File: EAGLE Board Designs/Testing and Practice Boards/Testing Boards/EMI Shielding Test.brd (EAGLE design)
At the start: 64.8 x 35.6 mm, 25 parts, among them J1 CONNECTOR-5_MICRO_VS_, J2 CONNECTOR-4_μF_S_RA_, U1 VOLTAGE_REGULATOR_ISO_MEE3_05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, U2 ISO224A, U3 VOLTAGE_REGULATOR_SOT-23-5_5V, U4 OPAMP_1_CHANNEL_OPA991

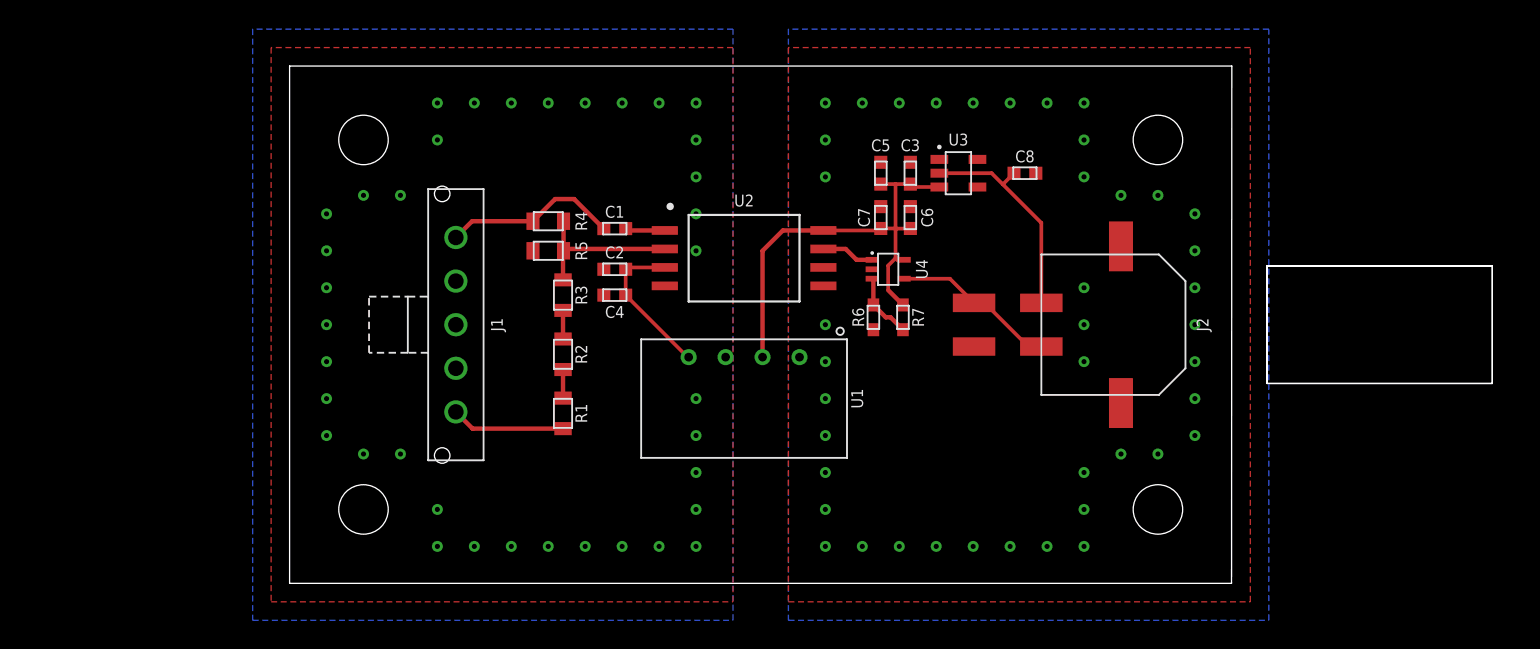
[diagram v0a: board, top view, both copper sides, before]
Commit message: fixed trace width
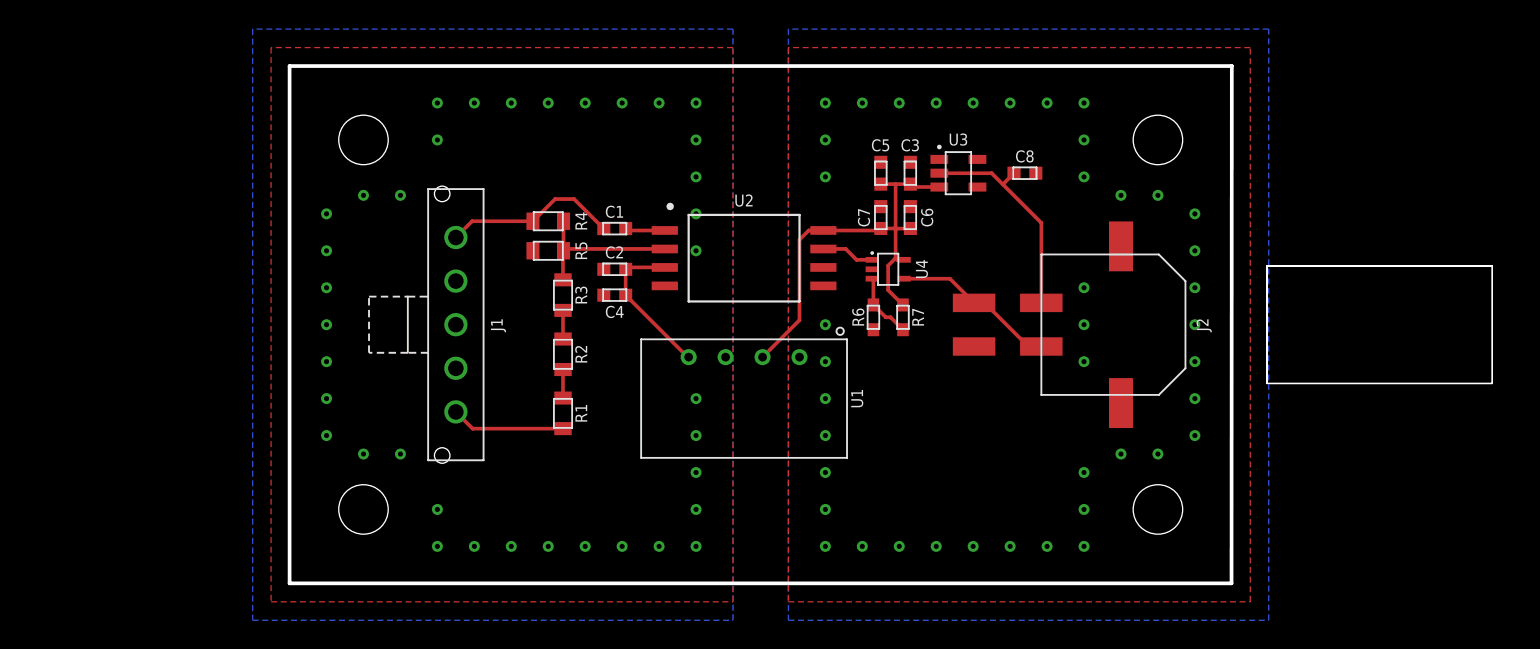
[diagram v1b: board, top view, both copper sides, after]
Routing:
- net +5V: track 31.8 -> 30.8 mm

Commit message: fixed spacing, changed connectors
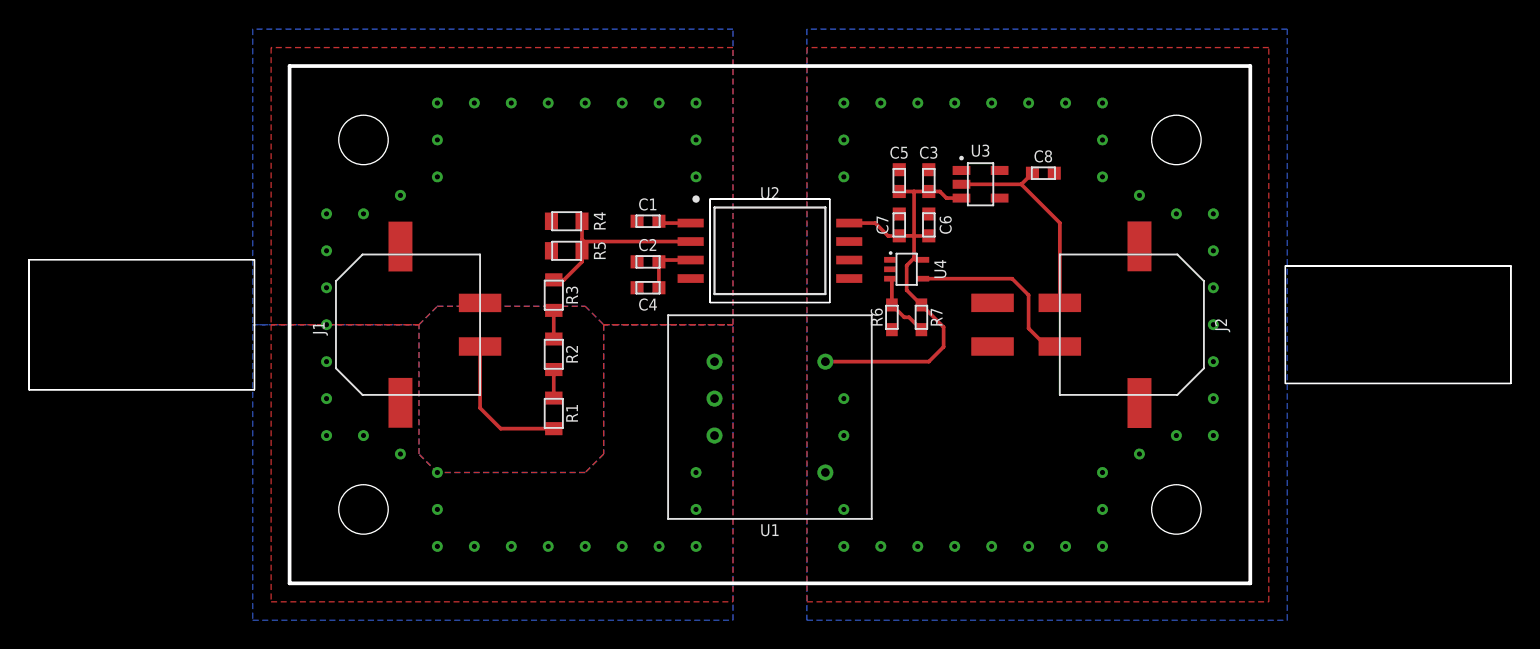
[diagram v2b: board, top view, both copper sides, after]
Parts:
- J1: value CONNECTOR-5_MICRO_VS_ -> CONNECTOR-2_MICROFIT_SMD_RIGHTANGLE_02_SINGLE_BLACK; device HyTechDevices:MOLEX_MICROFIT_PTH_VERTICAL_05_SINGLE -> HyTechDevices:MOLEX_MICROFIT_SMD_RIGHTANGLE_02_SINGLE
- U1: value VOLTAGE_REGULATOR_ISO_MEE3_0505 -> VOLTAGE_REGULATOR_ISO_PQP1-D_; device HyTechDevices:MEE3XXXXSC -> HyTechDevices:PQP1-D
- U2: value ISO224A -> ISO224A_AIRGAP; device HyTechDevices:SOIC-08(WIDE,0.295") -> HyTechDevices:SOIC-08(WIDE,0.295")-AIRGAP
- moved J1 3.81 mm to (7.62, 17.8), turned to 270 degrees
- moved C1 2.34 mm to (24.6, 24.9)
- moved C2 2.34 mm to (24.6, 22.1)
- moved C4 2.34 mm to (24.6, 20.3)
- moved U1 2.18 mm to (33.0, 11.4), turned to 90 degrees
- moved U2 1.85 mm to (33.0, 22.9)
- moved U3 1.70 mm to (47.5, 27.4)
- moved C3 1.37 mm to (43.9, 27.7)
- moved C6 1.37 mm to (43.9, 24.6)
- moved C5 1.37 mm to (41.9, 27.7)
- moved C7 1.37 mm to (41.9, 24.6)
- moved C8 1.27 mm to (51.8, 28.2)
- moved J2 1.27 mm to (58.4, 17.8)
- moved R6 1.27 mm to (41.4, 18.3)
- moved U$7 1.27 mm to (61.0, 30.5)
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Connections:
- net +5V: now also U1.4; no longer U1.2
- net GND: now also J2.3; no longer J2.4
- net TS+5V: now also U1.5; no longer U1.4
- net TS-UNFUSED: now also J1.2, U1.7; no longer J1.5, U1.3
- net TS_ACTIVE_GLV: no longer J2.3
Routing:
- net TS-UNFUSED: track 12.1 -> 0.00 mm, vias 37 -> 35
- net TS+5V: track 10.6 -> 4.01 mm
- net TS_GLV: track 3.67 -> 0.00 mm
- net TS+UNFUSED: track 7.84 -> 9.88 mm
- net TS_DIVIDED: track 11.1 -> 13.0 mm
- net TS_ACTIVE_GLV: track 11.4 -> 12.7 mm
- net +5V: track 30.8 -> 31.6 mm
- net +24V: track 15.0 -> 14.4 mm
- net N$1: track 2.74 -> 2.23 mm
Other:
- board size 64.8 x 35.6 mm -> 66 x 35.6 mm

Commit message: added silkscreen
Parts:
- added U$10: (no value), HyTechManufacturing:LOGO_GT_MEDIUM
- added U$11: (no value), HyTechManufacturing:LOGO_HYTECH_SMALL
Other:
- board text added: "HyTech Racing 2023 TSAL HV Sense Board Designed by Mikhail Allen"
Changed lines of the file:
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@@
 <setting verticaltext="up"/>
 </settings>
-<grid distance="10" unitdist="mil" unit="mil" style="lines" multiple="1" display="yes" altdistance="5" altunitdist="mil" altunit="mil"/>
+<grid distance="50" unitdist="mil" unit="mil" style="lines" multiple="1" display="yes" altdistance="5" altunitdist="mil" altunit="mil"/>
 <layers>
 <layer number="1" name="Top" color="4" fill="1" visible="yes" active="yes"/>
@@
 <vertex x="60.96" y="5.08"/>
 </polygon>
+<text x="60.96" y="16.51" size="0.8128" layer="22" font="vector" rot="MR0">HyTech Racing 2023
+TSAL HV Sense Board
+Designed by Mikhail Allen</text>
 </plain>
 <attributes>
@@
 <attribute name="NAME" x="63.627" y="17.78" size="0.8128" layer="25" rot="R270" align="bottom-center"/>
 </element>
+<element name="U$10" library="HyTechManufacturing" package="LOGO_GT_MEDIUM" value="" x="15.24" y="12.7" smashed="yes" rot="MR0"/>
+<element name="U$11" library="HyTechManufacturing" package="LOGO_HYTECH_SMALL" value="" x="21.59" y="20.32" smashed="yes" rot="MR0"/>
 </elements>
 <signals>
@@
 </board>
 </drawing>
+<compatibility>
+<note version="6.3" minversion="6.2.2" severity="warning">
+Since Version 6.2.2 text objects can contain more than one line,
+which will not be processed correctly with this version.
+</note>
+</compatibility>
 </eagle>
